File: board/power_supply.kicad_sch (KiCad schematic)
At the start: 36 parts, among them J1 USB, U1 IP5306, U2 TPS562201, U3 RT9069

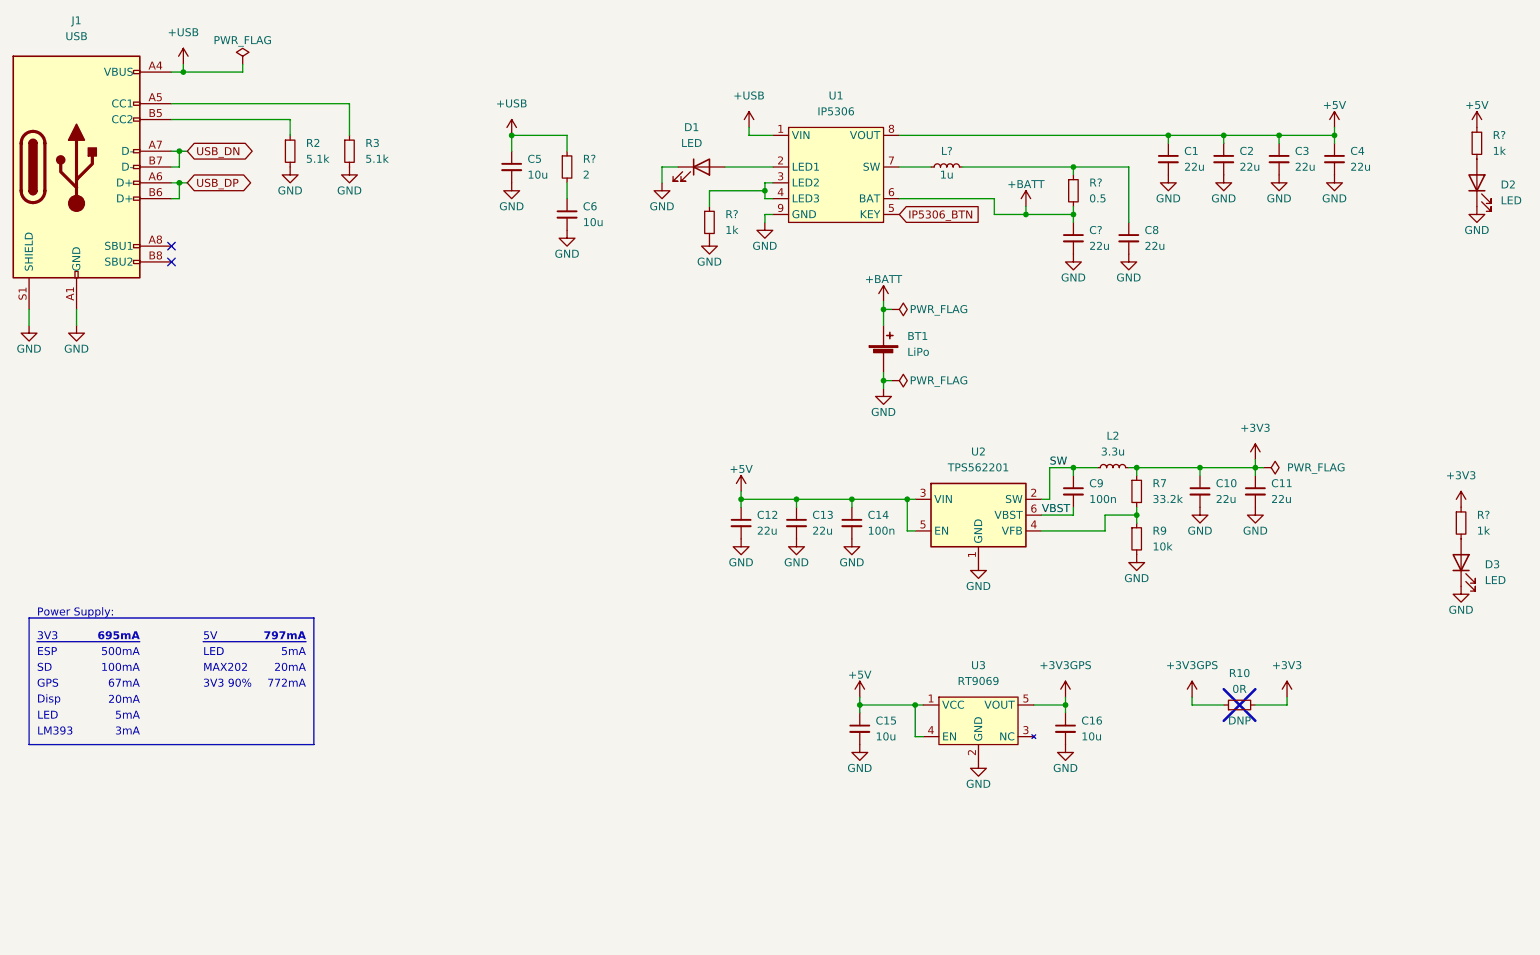
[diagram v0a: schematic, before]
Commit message: Updated price information for 10x and added a calculation for 20 boards including all parts and assembly cost
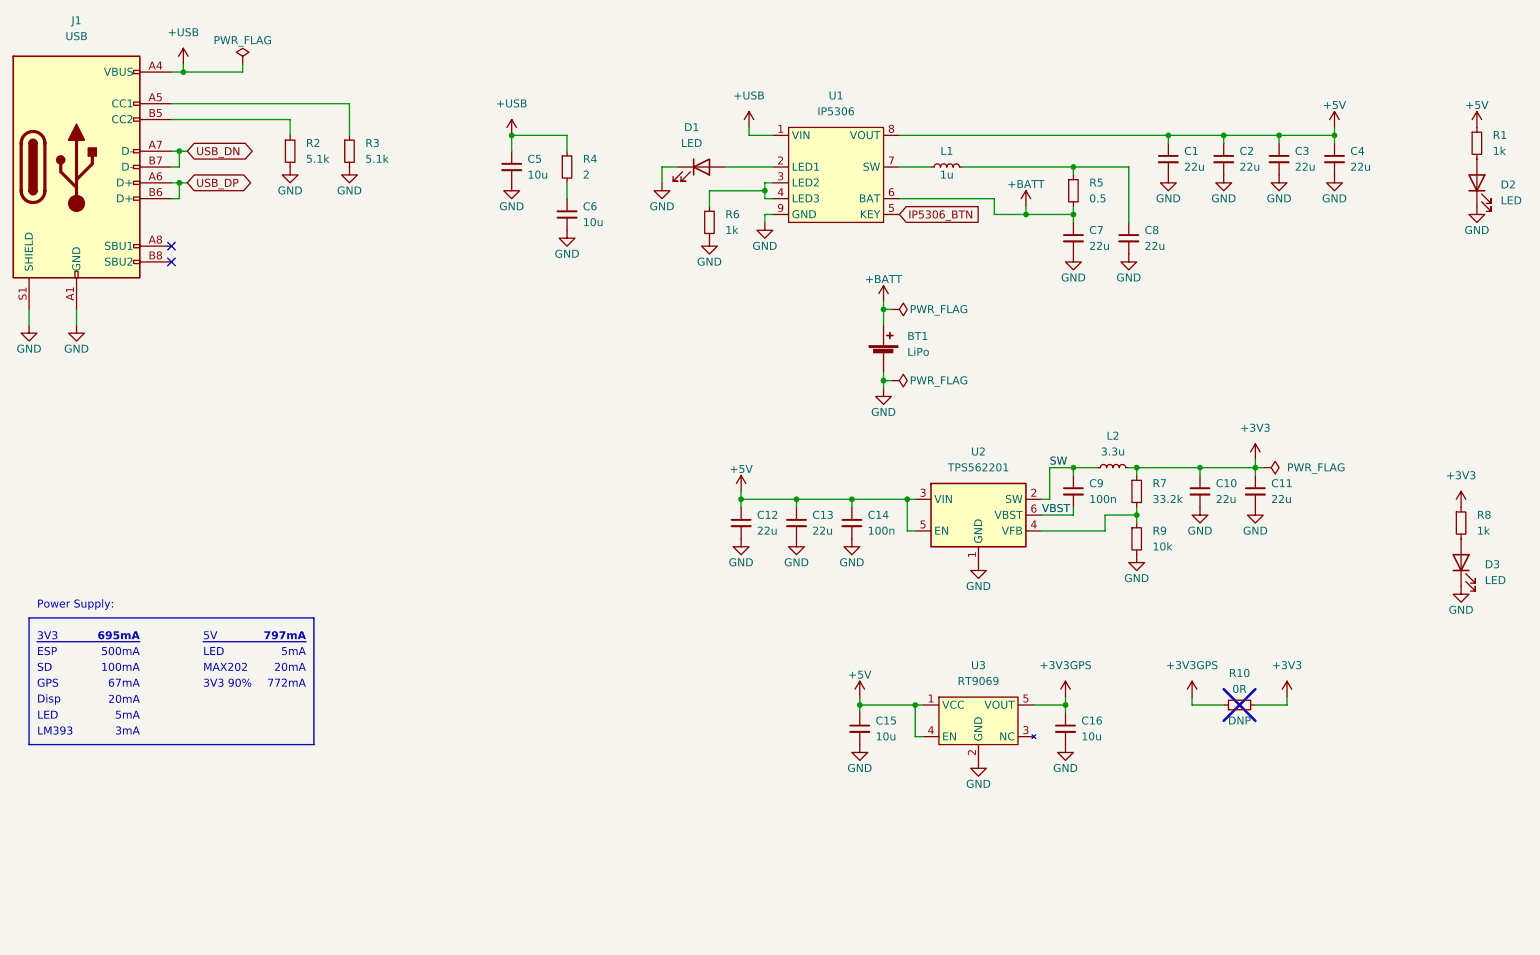
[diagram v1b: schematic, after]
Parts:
- BT1: JLC_Price10 (none) -> 0.0079
- C1, C10, C11, C12, C13, C2, C3, C4, C8: JLC_BasicPart yes -> no; JLC_Price10 (none) -> 0.0217
- C14, C9: JLC_Price10 0.0042 -> 0.0021
- C15, C16, C5, C6: JLC_Price10 0.0062 -> 0.0052
- C7: renamed from C?; JLC_BasicPart yes -> no; JLC_Price10 (none) -> 0.0217
- D1, D2, D3: JLC_Price10 0.0106 -> 0.0248
- J1: JLC_Price10 0.1309 -> 0.2007
- L1: renamed from L?; JLC_Price10 (none) -> 0.0815
- L2: JLC_Price10 (none) -> 0.0766
- R1, R6, R8: renamed from R?; JLC_Price10 (none) -> 0.0005
- R10: JLC_Price10 (none) -> 0.001
- R2, R3, R7: JLC_Price10 (none) -> 0.0009
- R4: renamed from R?; JLC_Price10 (none) -> 0.0012
- R5: renamed from R?; JLC_Price10 (none) -> 0.0025
- R9: JLC_Price10 (none) -> 0.0013
- U1: JLC_Price10 (none) -> 0.1766
- U2: JLC_Price10 (none) -> 0.1185
- U3: JLC_Price10 (none) -> 0.3239

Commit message: Updated schematic to new revision: Switch ultrasonic modules to PGA460, using ublox M10 GPS
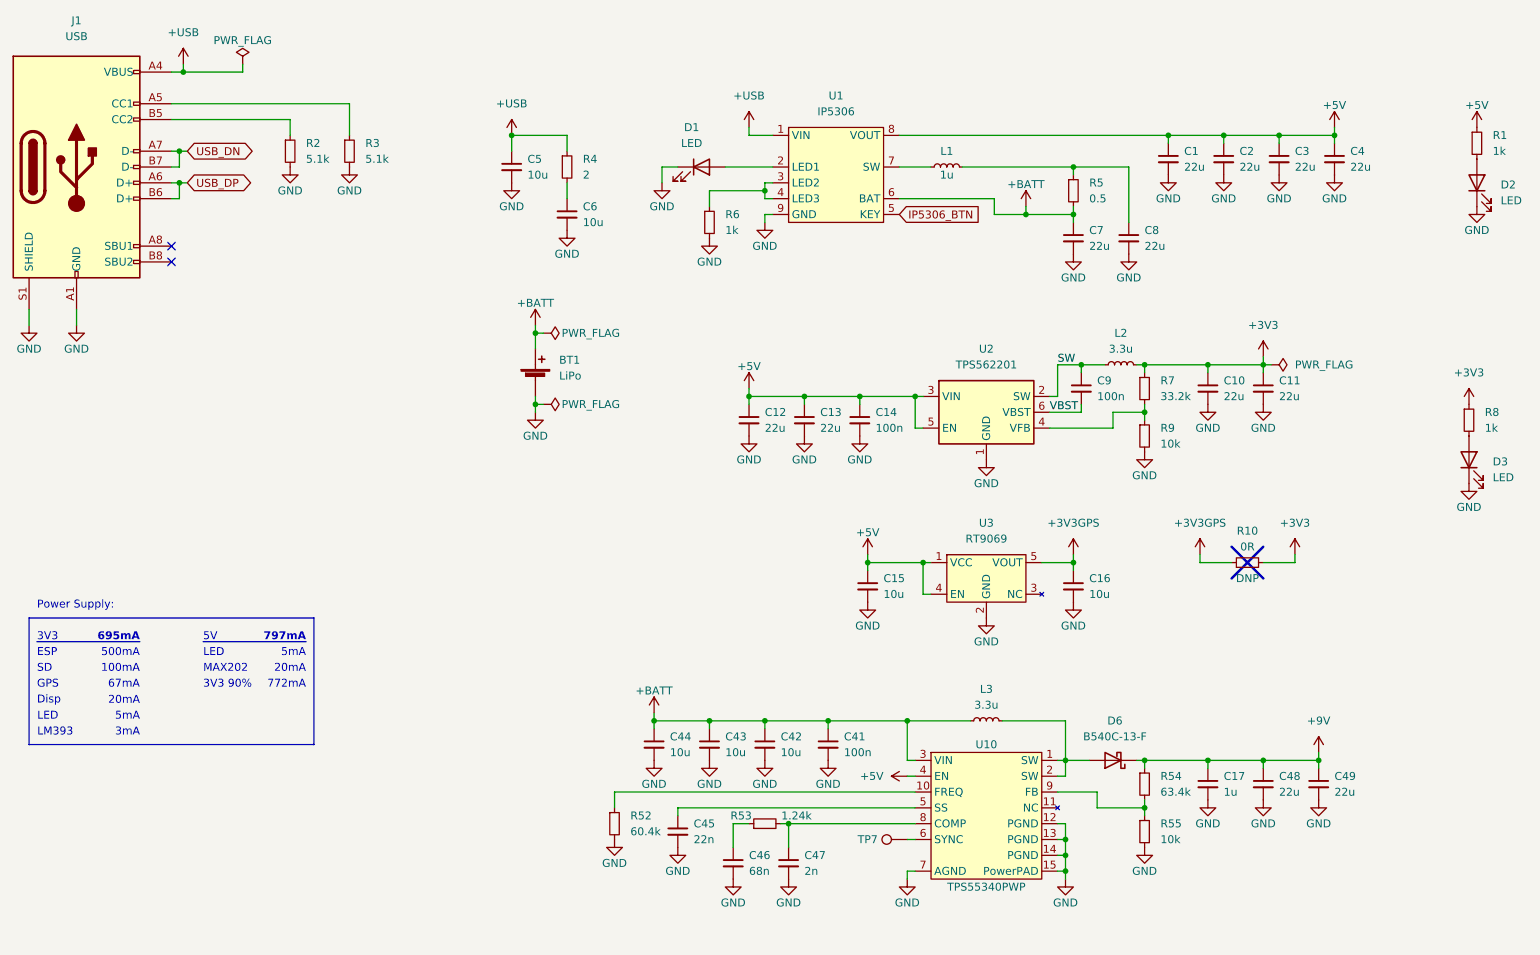
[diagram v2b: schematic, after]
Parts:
- added C17: 1u, Capacitor_SMD:C_0603_1608Metric, symbol Device:C_Small
- added C41: 100n, Capacitor_SMD:C_0603_1608Metric, symbol Device:C_Small
- added C42, C43, C44: 10u, Capacitor_SMD:C_0603_1608Metric, symbol Device:C_Small
- added C45: 22n, Capacitor_SMD:C_0603_1608Metric, symbol Device:C_Small
- added C46: 68n, Capacitor_SMD:C_0603_1608Metric, symbol Device:C_Small
- added C47: 2n, Capacitor_SMD:C_0603_1608Metric, symbol Device:C_Small
- added C48, C49: 22u, Capacitor_SMD:C_1206_3216Metric, symbol Device:C_Small
- added D6: B540C-13-F, Diode_SMD:D_SMC, symbol Device:D_Schottky
- added L3: 3.3u, Inductor_SMD:L_Sunlord_MWSA0503S, symbol Device:L_Small
- added R52: 60.4k, Resistor_SMD:R_0603_1608Metric, symbol Device:R_Small
- added R53: 1.24k, Resistor_SMD:R_0603_1608Metric, symbol Device:R_Small
- added R54: 63.4k, Resistor_SMD:R_0603_1608Metric, symbol Device:R_Small
- added R55: 10k, Resistor_SMD:R_0603_1608Metric, symbol Device:R_Small
- added TP7: TestPoint, symbol Connector:TestPoint
- added U10: TPS55340PWP, OBSPro:TSSOP-14-1EP_2.6x2.6mm_P0.65mm, symbol OBSPro:TPS55340PWP
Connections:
- net +5V: now also U10.4 (EN)
- net +BATT: now also C41.1, C42.1, C43.1, C44.1, L3.1, U10.3 (VIN)
- net GND: now also C17.2, C41.2, C42.2, C43.2, C44.2, C45.2, C46.2, C47.2, C48.2, C49.2, R52.2, R55.2, U10.12 (PGND), U10.13 (PGND), U10.14 (PGND), U10.15 (PowerPAD), U10.7 (AGND)
- new net: C47.1, R53.2, U10.8 (COMP)
- new net: C46.1, R53.1
- new net: D6.2 (A), L3.2, U10.1 (SW), U10.2 (SW)
- new net: R54.2, R55.1, U10.9 (FB)
- new net: R52.1, U10.10 (FREQ)
- new net: TP7.1, U10.6 (SYNC)
- new net: C45.1, U10.5 (SS)
- new net +9V: C17.1, C48.1, C49.1, D6.1 (K), R54.1
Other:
- moved on the sheet: BT1, C10, C11, C12, C13, C14, C15, C16, C9, D3, L2, R10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

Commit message: Fixed ERC errors
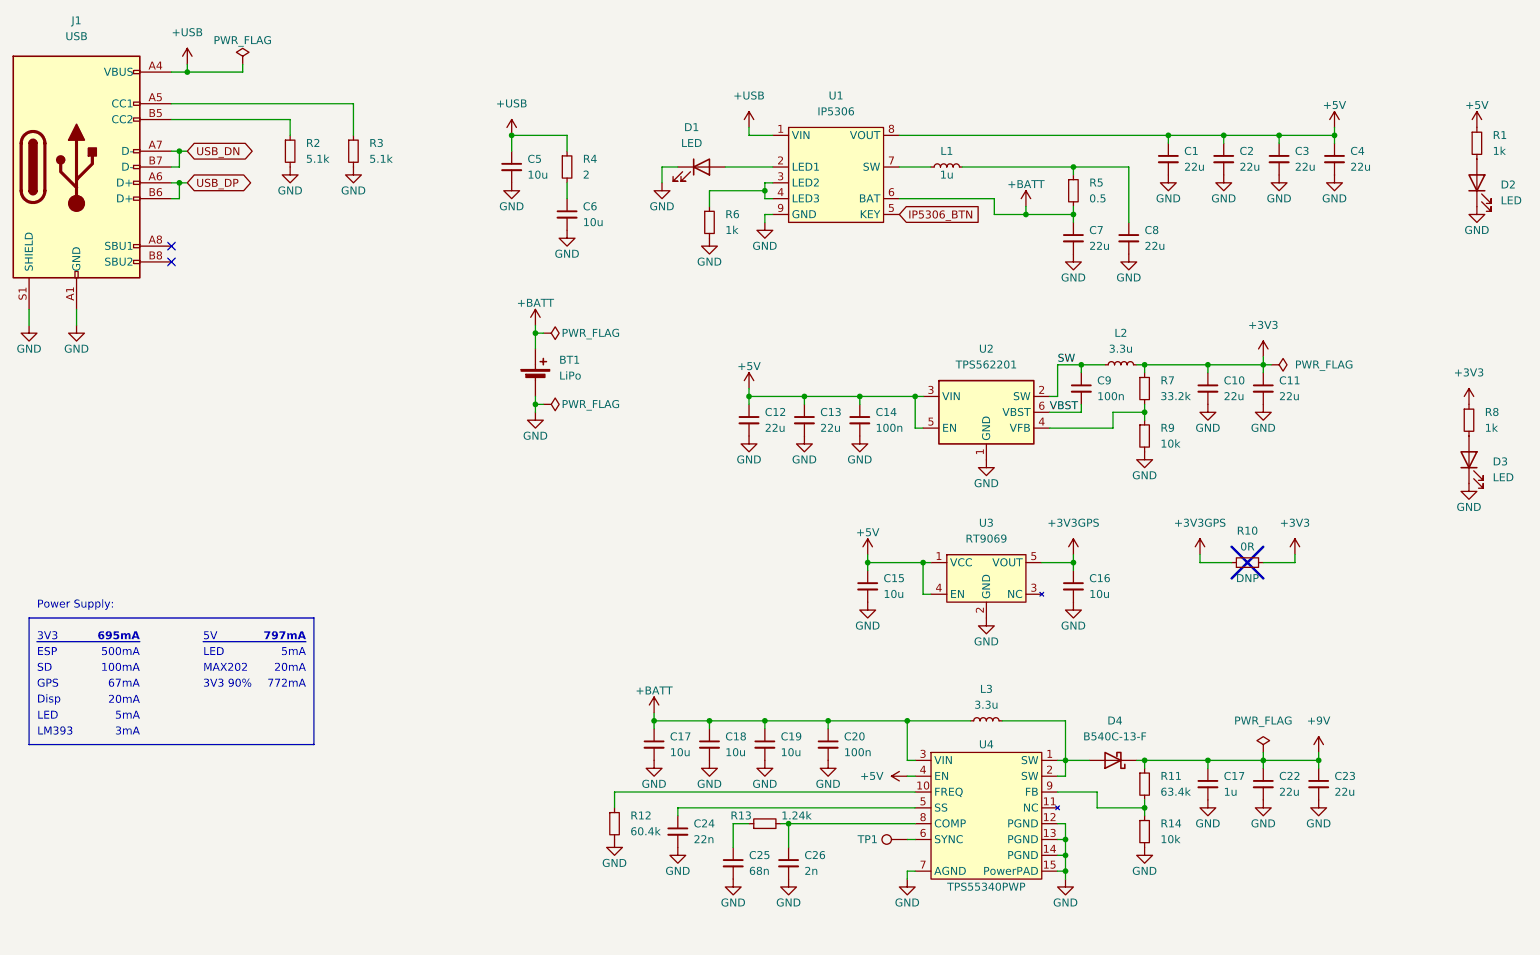
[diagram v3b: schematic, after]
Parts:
- TP1: renamed from TP7; footprint (none) -> TestPoint:TestPoint_Pad_1.0x1.0mm
- U4: renamed from U10; MPN TPS55340PWPR -> TPS55340PWP
- renumbered C44 to C17, C43 to C18, C42 to C19, C41 to C20, C48 to C22, C49 to C23, C45 to C24, C46 to C25, C47 to C26, D6 to D4, R54 to R11, R52 to R12, R53 to R13, R55 to R14
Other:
- moved on the sheet: R3

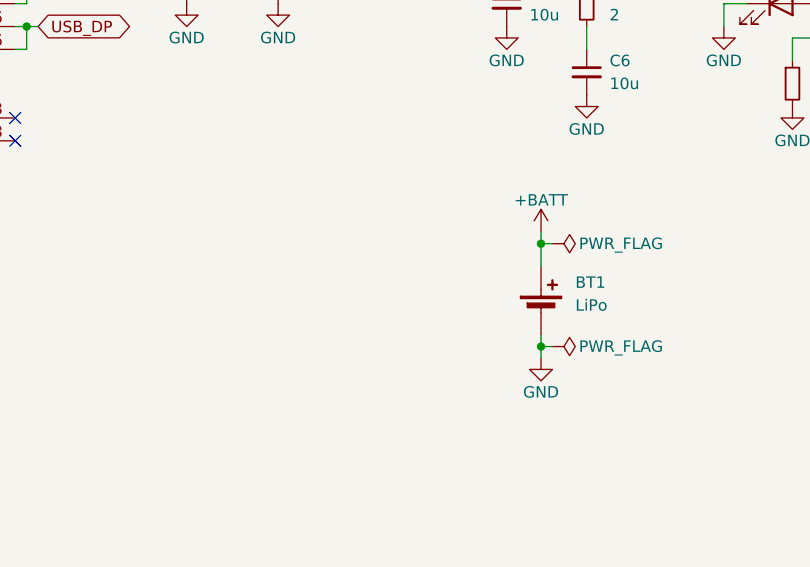
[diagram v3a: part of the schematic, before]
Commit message: Changed battery connector to JST PH 2.0mm
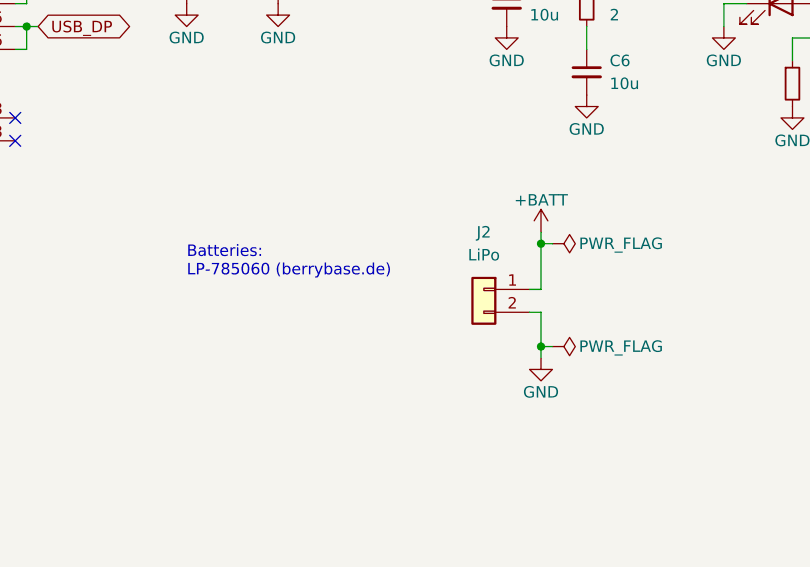
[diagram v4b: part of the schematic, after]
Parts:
- removed BT1: LiPo, OBSPro:PSS-254-2W, symbol Device:Battery_Cell
- added J2: LiPo, Connector_JST:JST_PH_S2B-PH-K_1x02_P2.00mm_Horizontal, symbol Connector_Generic:Conn_01x02
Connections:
- net +BATT: now also J2.1 (Pin_1)
- net GND: now also J2.2 (Pin_2)
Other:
- note added: "Batteries: LP-785060 (berrybase.de)"
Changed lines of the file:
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@@
     (stroke (width 0) (type default))
   )
+  (wire (pts (xy 109.22 76.2) (xy 110.49 76.2))
+    (stroke (width 0) (type default))
+  )
   (wire (pts (xy 212.09 36.83) (xy 212.09 38.1))
     (stroke (width 0) (type default))
@@
     (stroke (width 0) (type default))
   )
+  (wire (pts (xy 109.22 73.66) (xy 110.49 73.66))
+    (stroke (width 0) (type default))
+  )
   (wire (pts (xy 170.18 154.94) (xy 170.18 156.21))
     (stroke (width 0) (type default))
@@
     (stroke (width 0) (type default))
   )
-  (wire (pts (xy 110.49 68.58) (xy 110.49 71.12))
+  (wire (pts (xy 110.49 68.58) (xy 110.49 73.66))
     (stroke (width 0) (type default))
   )
@@
     (stroke (width 0) (type solid))
   )
-  (wire (pts (xy 110.49 80.01) (xy 110.49 78.74))
+  (wire (pts (xy 110.49 76.2) (xy 110.49 80.01))
     (stroke (width 0) (type default))
   )
@@
     (effects (font (size 1.27 1.27)) (justify left bottom))
   )
+  (text "Batteries:\nLP-785060 (berrybase.de)" (at 71.12 72.39 0)
+    (effects (font (size 1.27 1.27)) (justify left bottom))
+  )
   (text "20mA" (at 73.66 123.19 0)
     (effects (font (size 1.27 1.27)) (justify right bottom))
@@
     )
   )
-  (symbol (lib_id "Device:Battery_Cell") (at 110.49 76.2 0) (unit 1)
-    (in_bom yes) (on_board yes) (dnp no) (fields_autoplaced)
-    (property "Reference" "BT1" (at 114.3 72.8979 0)
-      (effects (font (size 1.27 1.27)) (justify left))
-    )
-    (property "Value" "LiPo" (at 114.3 75.4379 0)
-      (effects (font (size 1.27 1.27)) (justify left))
-    )
-    (property "Footprint" "OBSPro:PSS-254-2W" (at 110.49 74.676 90)
-      (effects (font (size 1.27 1.27)) hide)
-    )
-    (property "Datasheet" "~" (at 110.49 74.676 90)
-      (effects (font (size 1.27 1.27)) hide)
-    )
-    (property "JLC_PN" "C2979476" (at 110.49 76.2 0)
-      (effects (font (size 1.27 1.27)) hide)
-    )
-    (property "MPN" "HC-XH-2A-M" (at 110.49 76.2 0)
-      (effects (font (size 1.27 1.27)) hide)
-    )
-    (property "Manufacturer" "HCTL" (at 110.49 76.2 0)
-      (effects (font (size 1.27 1.27)) hide)
-    )
-    (property "JLC_BasicPart" "no" (at 110.49 76.2 0)
-      (effects (font (size 1.27 1.27)) hide)
-    )
-    (property "JLC_Price10" "0.0079" (at 110.49 76.2 0)
-      (effects (font (size 1.27 1.27)) hide)
-    )
-    (property "MF" "" (at 110.49 76.2 0)
-      (effects (font (size 1.27 1.27)) hide)
-    )
-    (property "Farnell_PN" "" (at 110.49 76.2 0)
-      (effects (font (size 1.27 1.27)) hide)
-    )
-    (property "Mouser_PN" "" (at 110.49 76.2 0)
-      (effects (font (size 1.27 1.27)) hide)
-    )
-    (pin "1")
-    (pin "2")
-    (instances
-      (project "OBSPro"
-        (path "/1b575199-a76e-4620-8a1a-43f78ed7da24/bd86e64d-47ab-4157-aab6-b537ca51decb"
-          (reference "BT1") (unit 1)
-        )
-      )
-    )
-  )
   (symbol (lib_id "Device:C_Small") (at 238.76 40.64 0) (unit 1)
     (in_bom yes) (on_board yes) (dnp no) (fields_autoplaced)
@@
   (symbol (lib_id "power:PWR_FLAG") (at 227.33 135.89 0) (unit 1)
     (in_bom yes) (on_board yes) (dnp no) (fields_autoplaced)
-    (property "Reference" "#FLG07" (at 227.33 133.985 0)
+    (property "Reference" "#FLG05" (at 227.33 133.985 0)
       (effects (font (size 1.27 1.27)) hide)
     )
@@
       (project "OBSPro"
         (path "/1b575199-a76e-4620-8a1a-43f78ed7da24/bd86e64d-47ab-4157-aab6-b537ca51decb"
-          (reference "#FLG07") (unit 1)
+          (reference "#FLG05") (unit 1)
         )
       )
@@
         )
       )
+    )
+  )
+  (symbol (lib_id "Connector_Generic:Conn_01x02") (at 104.14 73.66 0) (mirror y) (unit 1)
+    (in_bom yes) (on_board yes) (dnp no) (fields_autoplaced)
+    (property "Reference" "J2" (at 104.14 67.31 0)
+      (effects (font (size 1.27 1.27)))
+    )
+    (property "Value" "LiPo" (at 104.14 69.85 0)
+      (effects (font (size 1.27 1.27)))
+    )
+    (property "Footprint" "Connector_JST:JST_PH_S2B-PH-K_1x02_P2.00mm_Horizontal" (at 104.14 73.66 0)
+      (effects (font (size 1.27 1.27)) hide)
+    )
+    (property "Datasheet" "~" (at 104.14 73.66 0)
+      (effects (font (size 1.27 1.27)) hide)
+    )
+    (property "MPN" "S2B-PH-K-S(LF)(SN)" (at 104.14 73.66 0)
+      (effects (font (size 1.27 1.27)) hide)
+    )
+    (property "MF" "JST" (at 104.14 73.66 0)
+      (effects (font (size 1.27 1.27)) hide)
+    )
+    (property "Farnell_PN" "" (at 104.14 73.66 0)
+      (effects (font (size 1.27 1.27)) hide)
+    )
+    (property "Mouser_PN" "" (at 104.14 73.66 0)
+      (effects (font (size 1.27 1.27)) hide)
+    )
+    (property "JLC_PN" "C173752" (at 104.14 73.66 0)
+      (effects (font (size 1.27 1.27)) hide)
+    )
+    (pin "2")
+    (pin "1")
+    (instances
+      (project "OBSPro"
+        (path "/1b575199-a76e-4620-8a1a-43f78ed7da24/bd86e64d-47ab-4157-aab6-b537ca51decb"
+          (reference "J2") (unit 1)
+        )
+      )
